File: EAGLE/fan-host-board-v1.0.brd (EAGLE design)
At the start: 45.7 x 25.4 mm, 40 parts, among them J5 KK-254-4KK-254

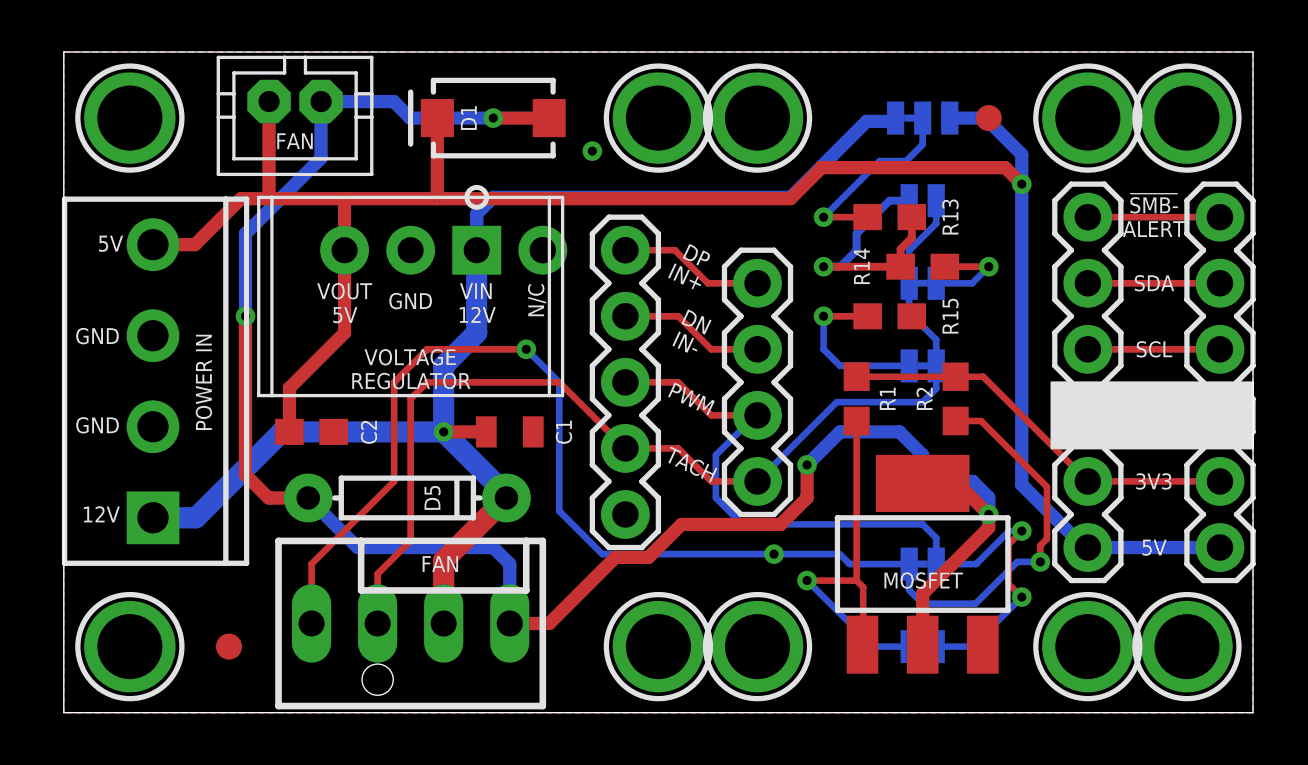
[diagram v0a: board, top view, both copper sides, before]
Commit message: fixes to the TACH lines
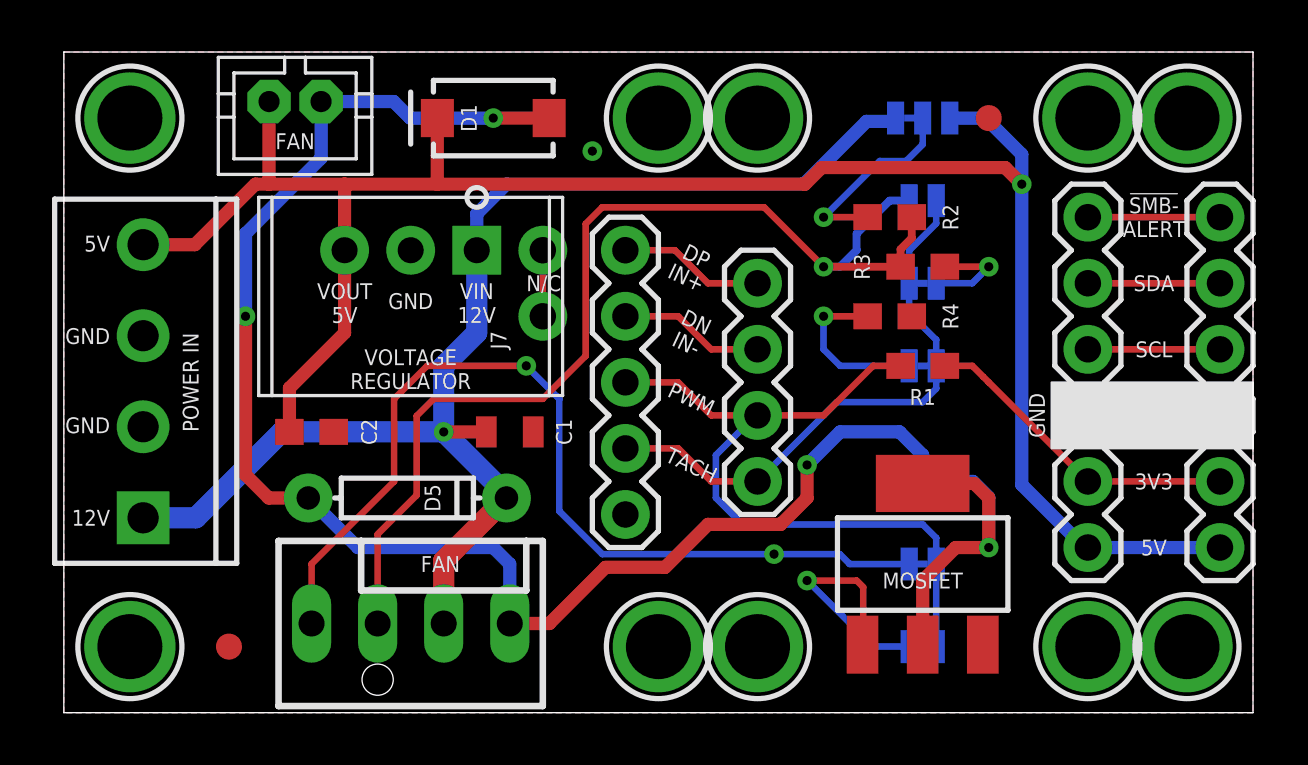
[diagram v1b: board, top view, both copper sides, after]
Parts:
- removed J8: (no value), SparkFun-Connectors:1X01_NO_SILK
- removed R13: 10k, SparkFun-Resistors:0603
- added J7: (no value), SparkFun-Connectors:1X02_NO_SILK
- R2: value 2.2k -> 10k
- moved R2 7.43 mm to (31.8, 19.1), turned to 0 degrees
- moved R1 2.84 mm to (33.0, 13.3), turned to 0 degrees
- moved J6 0.38 mm to (3.05, 7.49)
- renumbered J5 to 12V-FAN, R14 to R3, R15 to R4, U$13 to 5V-FAN
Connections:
- removed net N$1: JP2.2, R13.2, R3.1
- new net TACH/SENS: 12V-FAN.3:TACH, JP2.2, R2.2, R3.1
- net 3V3: no longer R2.1
- net N$2: no longer R1.1
- net N$4: now also R2.1; no longer R13.1
- net PWM: now also R1.1
- net PWM-F: no longer R2.2
- net SHDN: now also J7.1, J7.2; no longer J8.1
- net TACH: no longer 12V-FAN.3:TACH
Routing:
- net TACH/SENS: track 0.00 -> 41.2 mm, vias 0 -> 1
- net TACH: track 40.8 -> 22.0 mm
- net PWM-F: track 51.7 -> 36.0 mm, vias 3 -> 2
- net N$1: track 9.76 -> 0.00 mm, vias 1 -> 0
- net N$2: track 15.6 -> 9.46 mm
- net 3V3: track 15.6 -> 12.4 mm
- net SHDN: track 0.00 -> 2.54 mm
- net GND-3: track 11.6 -> 13.9 mm
- net PWM: track 30.5 -> 29.1 mm, vias 2 -> 0
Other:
- board text added: "Rev. 1.0"

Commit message: minor edits
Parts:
- moved U$14 1.27 mm to (33.0, 6.99)
- renumbered U$2 to VREG
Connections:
- new net ALERT: J4.6
- net !SMBALERT: no longer J4.6
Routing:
- net !SMBALERT: track 5.08 -> 0.00 mm
- net N$2: track 9.46 -> 7.67 mm
- net GND-3: track 13.9 -> 14.4 mm
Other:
- board text added: "ALERT"
- board text removed: "!SMB- ALERT"
- board text removed: "ALERT !SMB-A"
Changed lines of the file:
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@@
 for AMC6821 &amp;
 EMC2101 breakout boards</text>
-<text x="41.91" y="19.05" size="0.6096" layer="26" rot="MR0" align="center">ALERT
-!SMB-A</text>
+<text x="41.91" y="19.05" size="0.6096" layer="26" rot="MR0" align="center">ALERT</text>
 <text x="41.91" y="16.51" size="0.6096" layer="26" rot="MR0" align="center">SDA</text>
 <text x="41.91" y="13.97" size="0.6096" layer="26" rot="MR0" align="center">SCL</text>
@@
 <text x="37.846" y="11.557" size="0.6096" layer="26" rot="MR270" align="bottom-center">GND</text>
 <text x="5.334" y="12.7" size="0.6096" layer="26" rot="MR90" align="bottom-center">GND</text>
-<text x="20.32" y="6.35" size="0.6096" layer="26" rot="MR0" align="center-left">(c) 2021 Tecsmith / Vino Rodrigues</text>
+<text x="20.32" y="6.604" size="0.6096" layer="26" rot="MR0" align="center-left">(c) 2021 Tecsmith / Vino Rodrigues</text>
 <text x="24.13" y="17.145" size="0.6096" layer="25" rot="R335" align="center">DP
 IN+</text>
@@
 <text x="41.91" y="8.89" size="0.6096" layer="25" align="center">3V3</text>
 <text x="41.91" y="6.35" size="0.6096" layer="25" align="center">5V</text>
-<text x="41.91" y="19.05" size="0.6096" layer="25" align="center">!SMB-
-ALERT</text>
+<text x="41.91" y="19.05" size="0.6096" layer="25" align="center">ALERT</text>
 <text x="15.875" y="16.51" size="0.6096" layer="25" rot="R180" align="bottom-center">VIN
 12V</text>
@@
 <text x="13.335" y="13.97" size="0.6096" layer="25" align="top-center">VOLTAGE
 REGULATOR</text>
-<text x="33.02" y="5.08" size="0.6096" layer="25" align="center">MOSFET</text>
+<text x="33.02" y="7.62" size="0.6096" layer="25" align="center">MOSFET</text>
 <text x="4.572" y="12.7" size="0.6096" layer="25" rot="R270" align="bottom-center">POWER IN</text>
 <text x="8.89" y="21.971" size="0.6096" layer="25" align="center">FAN</text>
@@
 <attribute name="BOM" value="EXCLUDE" x="39.37" y="22.86" size="1.778" layer="27" display="off"/>
 </element>
-<element name="U$2" library="VinoRodrigues_Custom_Eagle" package="TRACO-TSR-1" value="TRACOPOWER-TSR-1" x="13.335" y="17.78" smashed="yes" rot="R180"/>
+<element name="VREG" library="VinoRodrigues_Custom_Eagle" package="TRACO-TSR-1" value="TRACOPOWER-TSR-1" x="13.335" y="17.78" smashed="yes" rot="R180"/>
 <element name="5V-FAN" library="VinoRodrigues_Custom_Eagle" package="JST-PH2" value="JST-PH-2" x="8.89" y="23.495" smashed="yes" rot="R180"/>
 <element name="JP3" library="SparkFun-Jumpers" package="SMT-JUMPER_2_NC_TRACE_SILK" package3d_urn="urn:adsk.eagle:package:39281/1" value="JUMPER-12V-a" x="33.02" y="16.51" smashed="yes" rot="MR180">
@@
 <attribute name="VALUE" x="33.02" y="19.177" size="0.4064" layer="28" font="vector" ratio="10" rot="MR0" align="top-center"/>
 </element>
-<element name="U$14" library="VinoRodrigues_Custom_Eagle" package="SOT223" value="NDT3055L" x="33.02" y="5.715" smashed="yes">
-<attribute name="VALUE" x="30.48" y="4.3942" size="0.4064" layer="27"/>
+<element name="U$14" library="VinoRodrigues_Custom_Eagle" package="SOT223" value="NDT3055L" x="33.02" y="6.985" smashed="yes">
+<attribute name="VALUE" x="30.48" y="5.6642" size="0.4064" layer="27"/>
 </element>
 <element name="JP5" library="SparkFun-Jumpers" package="SMT-JUMPER_3_1-NC_TRACE_SILK" package3d_urn="urn:adsk.eagle:package:39288/1" value="JUMPER-FAN-GND" x="33.02" y="8.89" smashed="yes" rot="MR0">
@@
 </element>
 <element name="R1" library="SparkFun-Resistors" package="0603" value="2.2k" x="33.02" y="13.335" smashed="yes">
-<attribute name="NAME" x="33.02" y="12.446" size="0.6096" layer="25" font="vector" ratio="20" rot="R180" align="bottom-center"/>
+<attribute name="NAME" x="31.115" y="13.335" size="0.6096" layer="25" font="vector" ratio="20" rot="R90" align="bottom-center"/>
 <attribute name="PROD_ID" value="RES-08272" x="33.02" y="13.335" size="1.778" layer="27" display="off"/>
 <attribute name="VALUE" x="33.02" y="12.573" size="0.6096" layer="27" font="vector" ratio="20" align="top-center"/>
@@
 </element>
 <element name="J7" library="SparkFun-Connectors" package="1X02_NO_SILK" value="" x="18.415" y="15.24" smashed="yes" rot="R90">
-<attribute name="NAME" x="17.018" y="13.97" size="0.6096" layer="25" font="vector" ratio="20" rot="R90"/>
 <attribute name="VALUE" x="20.447" y="13.97" size="0.6096" layer="27" font="vector" ratio="20" rot="R90"/>
 </element>
@@
 <signal name="12V">
 <contactref element="C1" pad="1"/>
-<contactref element="U$2" pad="P$+VIN"/>
+<contactref element="VREG" pad="P$+VIN"/>
 <contactref element="JP1" pad="3"/>
 <contactref element="12V-FAN" pad="2:+12VDC"/>
@@
 <signal name="5V">
 <contactref element="C2" pad="1"/>
-<contactref element="U$2" pad="P$+VOUT"/>
+<contactref element="VREG" pad="P$+VOUT"/>
 <contactref element="JP1" pad="1"/>
 <contactref element="5V-FAN" pad="1"/>
@@
 </signal>
 <signal name="GND">
-<contactref element="U$2" pad="P$GND"/>
+<contactref element="VREG" pad="P$GND"/>
 <contactref element="C1" pad="2"/>
 <contactref element="C2" pad="2"/>
@@
 <signal name="!SMBALERT">
 <contactref element="J2" pad="6"/>
-<contactref element="J4" pad="6"/>
-<wire x1="39.37" y1="19.05" x2="44.45" y2="19.05" width="0.254" layer="1"/>
 </signal>
 <signal name="SDA">
@@
 <contactref element="U$14" pad="G"/>
 <contactref element="JP7" pad="2"/>
-<wire x1="30.48" y1="5.08" x2="30.734" y2="4.826" width="0.254" layer="1"/>
-<wire x1="30.734" y1="4.826" x2="30.734" y2="2.641" width="0.254" layer="1"/>
-<wire x1="30.734" y1="2.641" x2="30.709" y2="2.616" width="0.254" layer="1"/>
+<wire x1="30.734" y1="3.937" x2="30.734" y2="3.911" width="0.254" layer="1"/>
+<wire x1="30.734" y1="3.911" x2="30.709" y2="3.886" width="0.254" layer="1"/>
 <wire x1="32.4993" y1="2.54" x2="31.115" y2="2.54" width="0.254" layer="16"/>
 <wire x1="31.115" y1="2.54" x2="28.575" y2="5.08" width="0.254" layer="16"/>
 <via x="28.575" y="5.08" extent="1-16" drill="0.35"/>
-<wire x1="28.575" y1="5.08" x2="30.48" y2="5.08" width="0.254" layer="1"/>
+<wire x1="28.575" y1="5.08" x2="29.718" y2="3.937" width="0.254" layer="1"/>
+<wire x1="30.734" y1="3.937" x2="29.718" y2="3.937" width="0.254" layer="1"/>
 </signal>
 <signal name="GND-3">
@@
 <wire x1="35.56" y1="8.2804" x2="34.9504" y2="8.89" width="0.508" layer="16"/>
 <via x="35.56" y="6.35" extent="1-16" drill="0.35"/>
-<wire x1="35.56" y1="6.35" x2="34.29" y2="6.35" width="0.508" layer="1"/>
-<wire x1="34.29" y1="6.35" x2="33.02" y2="5.08" width="0.508" layer="1"/>
-<wire x1="33.02" y1="5.08" x2="33.02" y2="2.616" width="0.508" layer="1"/>
-<wire x1="35.56" y1="6.35" x2="35.56" y2="8.255" width="0.508" layer="1"/>
-<wire x1="35.56" y1="8.255" x2="35.001" y2="8.814" width="0.508" layer="1"/>
-<wire x1="33.02" y1="8.814" x2="35.001" y2="8.814" width="0.508" layer="1"/>
+<wire x1="35.56" y1="6.35" x2="33.528" y2="6.35" width="0.508" layer="1"/>
+<wire x1="33.528" y1="6.35" x2="33.02" y2="5.842" width="0.508" layer="1"/>
+<wire x1="33.02" y1="5.842" x2="33.02" y2="3.886" width="0.508" layer="1"/>
+<wire x1="35.56" y1="6.35" x2="35.56" y2="9.652" width="0.508" layer="1"/>
+<wire x1="35.56" y1="9.652" x2="35.128" y2="10.084" width="0.508" layer="1"/>
+<wire x1="33.02" y1="10.084" x2="35.128" y2="10.084" width="0.508" layer="1"/>
 </signal>
 <signal name="PWM-F">
@@
 <wire x1="13.5664" y1="8.3594" x2="12.065" y2="6.858" width="0.254" layer="1"/>
 </signal>
+<signal name="ALERT">
+<contactref element="J4" pad="6"/>
+</signal>
 </signals>

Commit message: updates
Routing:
- net N$2: track 7.67 -> 5.45 mm
- net TACH/SENS: track 41.2 -> 40.0 mm
- net GND-3: track 14.4 -> 15.2 mm, vias 1 -> 2
- net N$6: track 6.51 -> 5.77 mm
- net PWM-F: track 36.0 -> 36.4 mm, vias 2 -> 1
- net GND-F: track 59.5 -> 59.7 mm, vias 3 -> 4

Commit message: updates
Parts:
- removed FID3, FID4: FIDUCIAL_1MM, microbuilder:FIDUCIAL_1MM
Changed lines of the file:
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@@
 <attribute name="BOM" value="EXCLUDE" x="17.78" y="17.78" size="1.778" layer="27" display="off"/>
-</element>
-<element name="FID3" library="microbuilder" package="FIDUCIAL_1MM" value="FIDUCIAL_1MM" x="6.35" y="2.54" smashed="yes">
-<attribute name="BOM" value="EXCLUDE" x="6.35" y="2.54" size="1.778" layer="27" display="off"/>
-</element>
-<element name="FID4" library="microbuilder" package="FIDUCIAL_1MM" value="FIDUCIAL_1MM" x="35.56" y="22.86" smashed="yes">
-<attribute name="BOM" value="EXCLUDE" x="33.02" y="20.32" size="1.778" layer="27" display="off"/>
 </element>
 <element name="U$8" library="microbuilder" package="MOUNTINGHOLE_2.5_PLATED" value="MOUNTINGHOLE2.5" x="43.18" y="2.54" smashed="yes">
